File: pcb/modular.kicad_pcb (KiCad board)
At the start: 2 copper layers, 60 x 52 mm, 0 parts

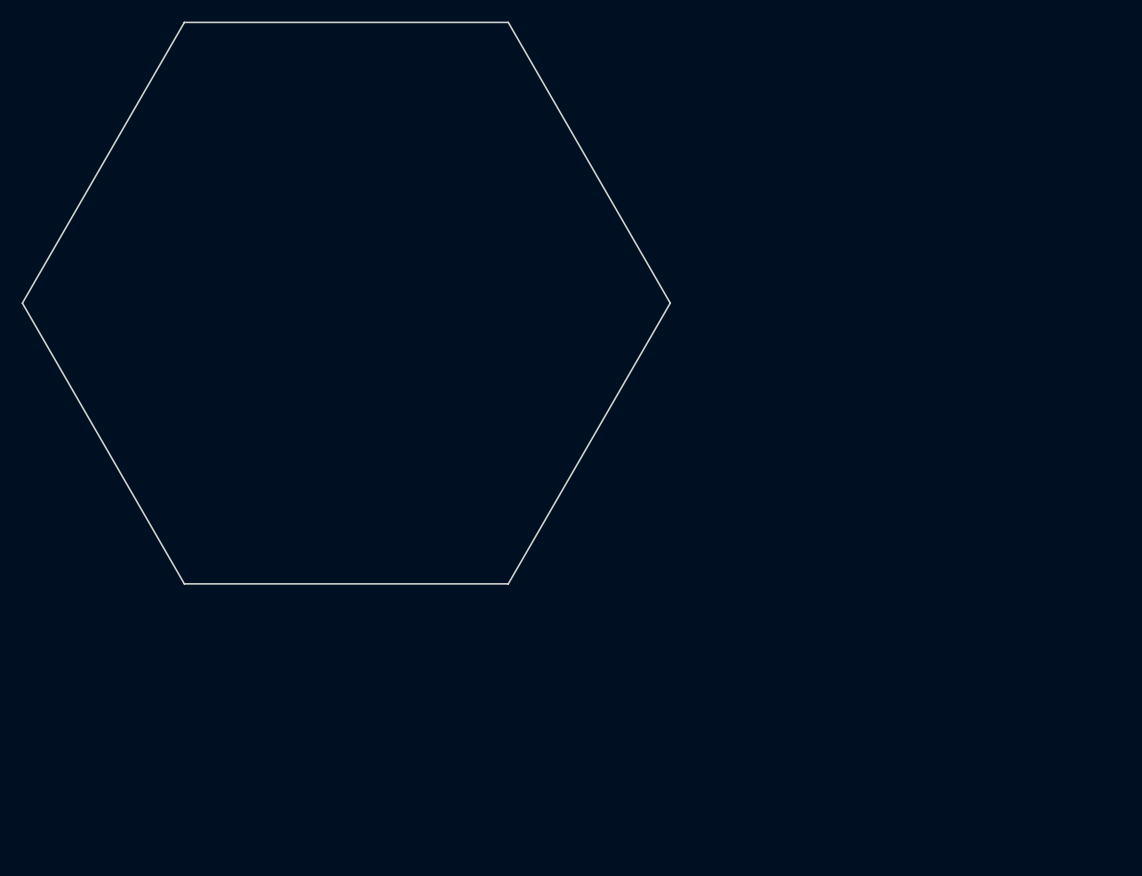
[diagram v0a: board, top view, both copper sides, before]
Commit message: Added pcb layout
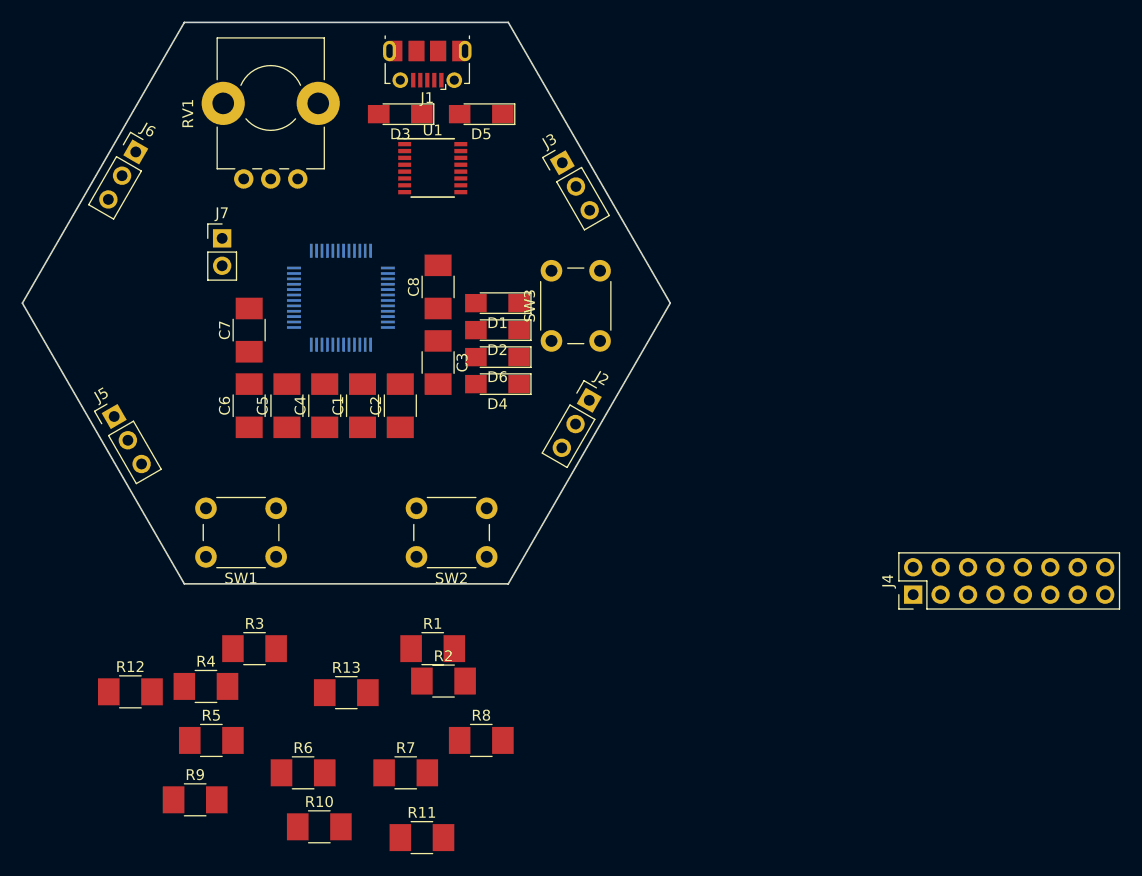
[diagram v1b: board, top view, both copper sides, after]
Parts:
- added C1: 47p, Capacitors_SMD:C_1210_HandSoldering, F.Cu at (163.5, 129.5)
- added C2: 47p, Capacitors_SMD:C_1210_HandSoldering, F.Cu at (167.0, 129.5)
- added C3: 100n, Capacitors_SMD:C_1210_HandSoldering, F.Cu at (170.5, 125.5)
- added C4: 100n, Capacitors_SMD:C_1210_HandSoldering, F.Cu at (160.0, 129.5)
- added C5: 100n, Capacitors_SMD:C_1210_HandSoldering, F.Cu at (156.5, 129.5)
- added C6: 4.7u, Capacitors_SMD:C_1210_HandSoldering, F.Cu at (153.0, 129.5)
- added C7: 100n, Capacitors_SMD:C_1210_HandSoldering, F.Cu at (153.0, 122.5)
- added C8: C, Capacitors_SMD:C_1210_HandSoldering, F.Cu at (170.5, 118.5)
- added D1: LED, LEDs:LED_1206_HandSoldering, F.Cu at (176.0, 120.0)
- added D2: LED, LEDs:LED_1206_HandSoldering, F.Cu at (176.0, 122.5)
- added D3: RXLED, LEDs:LED_1206_HandSoldering, F.Cu at (167.0, 102.5)
- added D4: LED, LEDs:LED_1206_HandSoldering, F.Cu at (176.0, 127.5)
- added D5: TXLED, LEDs:LED_1206_HandSoldering, F.Cu at (174.5, 102.5)
- added D6: LED, LEDs:LED_1206_HandSoldering, F.Cu at (176.0, 125.0)
- added J1: USB_OTG, Connectors_USB:USB_Micro-B_Molex-105017-0001, F.Cu at (169.5, 97.0)
- added J2: OUTPUT1, Pin_Headers:Pin_Header_Straight_1x03_Pitch2.54mm, F.Cu at (184.5, 129.0)
- added J3: OUTPUT2, Pin_Headers:Pin_Header_Straight_1x03_Pitch2.54mm, F.Cu at (182.0, 107.0)
- added J4: GPIO, Pin_Headers:Pin_Header_Straight_2x08_Pitch2.54mm, F.Cu at (214.5, 147.0)
- added J5: INPUT1, Pin_Headers:Pin_Header_Straight_1x03_Pitch2.54mm, F.Cu at (140.5, 130.5)
- added J6: INPUT2, Pin_Headers:Pin_Header_Straight_1x03_Pitch2.54mm, F.Cu at (142.5, 106.0)
- added J7: BOOT, Pin_Headers:Pin_Header_Straight_1x02_Pitch2.54mm, F.Cu at (150.5, 114.0)
- added R1: 10k, Resistors_SMD:R_1210_HandSoldering, F.Cu at (170.0, 152.0)
- added R10: 270, Resistors_SMD:R_1210_HandSoldering, F.Cu at (159.5, 168.5)
- added R11: 270, Resistors_SMD:R_1210_HandSoldering, F.Cu at (169.0, 169.5)
- added R12: 270, Resistors_SMD:R_1210_HandSoldering, F.Cu at (142.0, 156.0)
- added R13: 4k7, Resistors_SMD:R_1210_HandSoldering, F.Cu at (162.0, 156.1)
- added R2: 4k7, Resistors_SMD:R_1210_HandSoldering, F.Cu at (171.0, 155.0)
- added R3: 27, Resistors_SMD:R_1210_HandSoldering, F.Cu at (153.5, 152.0)
- added R4: 27, Resistors_SMD:R_1210_HandSoldering, F.Cu at (149.0, 155.5)
- added R5: 270, Resistors_SMD:R_1210_HandSoldering, F.Cu at (149.5, 160.5)
- added R6: 4k7, Resistors_SMD:R_1210_HandSoldering, F.Cu at (158.0, 163.5)
- added R7: 4k7, Resistors_SMD:R_1210_HandSoldering, F.Cu at (167.5, 163.5)
- added R8: 270, Resistors_SMD:R_1210_HandSoldering, F.Cu at (174.5, 160.5)
- added R9: 270, Resistors_SMD:R_1210_HandSoldering, F.Cu at (148.0, 166.0)
- added RV1: KNOB, Potentiometers:Potentiometer_Alps_RK09K_Horizontal, F.Cu at (157.5, 108.5)
- added SW1: BTN1, Buttons_Switches_THT:SW_PUSH_6mm, F.Cu at (155.5, 143.5)
- added SW2: BTN2, Buttons_Switches_THT:SW_PUSH_6mm, F.Cu at (175.0, 143.5)
- added SW3: RESET, Buttons_Switches_THT:SW_PUSH_6mm, F.Cu at (181.0, 123.5)
- added U1: FT230XS-R, Housings_SSOP:SSOP-16_3.9x4.9mm_Pitch0.635mm, F.Cu at (170.0, 107.5)
- added U2: STM32F302CCTx, Housings_QFP:LQFP-48_7x7mm_Pitch0.5mm, B.Cu at (161.5, 119.5)

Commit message: Moved all components onto board. First rev.
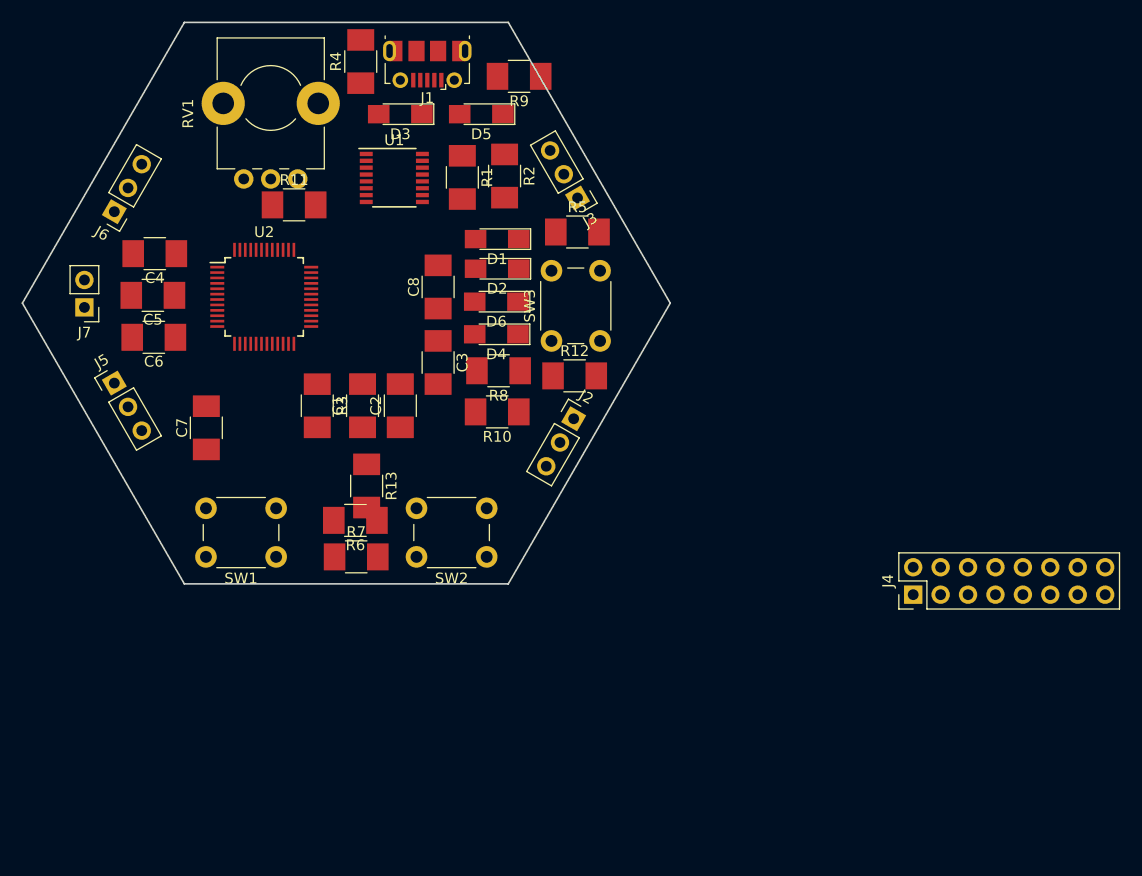
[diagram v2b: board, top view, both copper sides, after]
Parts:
- U2: moved to F.Cu
- moved R9 73.4 mm to (178.0, 99.0), turned to 180 degrees
- moved R11 59.8 mm to (157.2, 110.9)
- moved R4 59.6 mm to (163.3, 97.6), turned to 90 degrees
- moved R5 58.0 mm to (183.4, 113.4)
- moved R12 50.5 mm to (183.1, 126.7)
- moved R2 47.1 mm to (176.7, 108.2), turned to 270 degrees
- moved R1 43.7 mm to (172.7, 108.4), turned to 270 degrees
- moved R10 41.8 mm to (176.0, 130.1), turned to 180 degrees
- moved R8 34.3 mm to (176.1, 126.3), turned to 180 degrees
- moved R6 23.9 mm to (162.8, 140.1), turned to 180 degrees
- moved R3 23.2 mm to (159.3, 129.5), turned to 270 degrees
- moved C4 21.1 mm to (144.3, 115.4), turned to 180 degrees
- moved R7 20.5 mm to (162.9, 143.5)
- moved R13 19.2 mm to (163.9, 136.9), turned to 270 degrees
- moved C5 16.1 mm to (144.1, 119.3), turned to 180 degrees
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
